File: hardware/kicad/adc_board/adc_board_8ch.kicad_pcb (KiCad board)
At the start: 2 copper layers, 88 x 66 mm, 10 parts, among them J1 ELECTRODES, J2 SPI_HOST, J3 PWR_CTRL, U1 ADS131M08

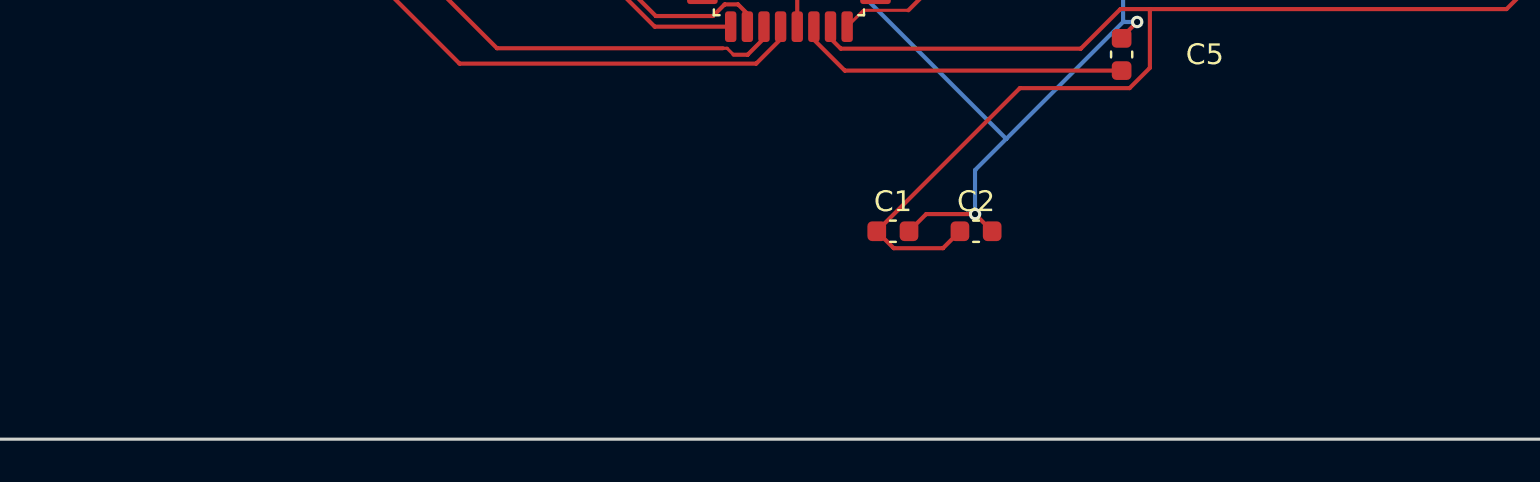
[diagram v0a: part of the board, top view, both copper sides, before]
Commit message: feat: add GND-tied fractal fill to ADC board
Co-authored-by: Copilot <223556219+Copilot@users.noreply.github.com>
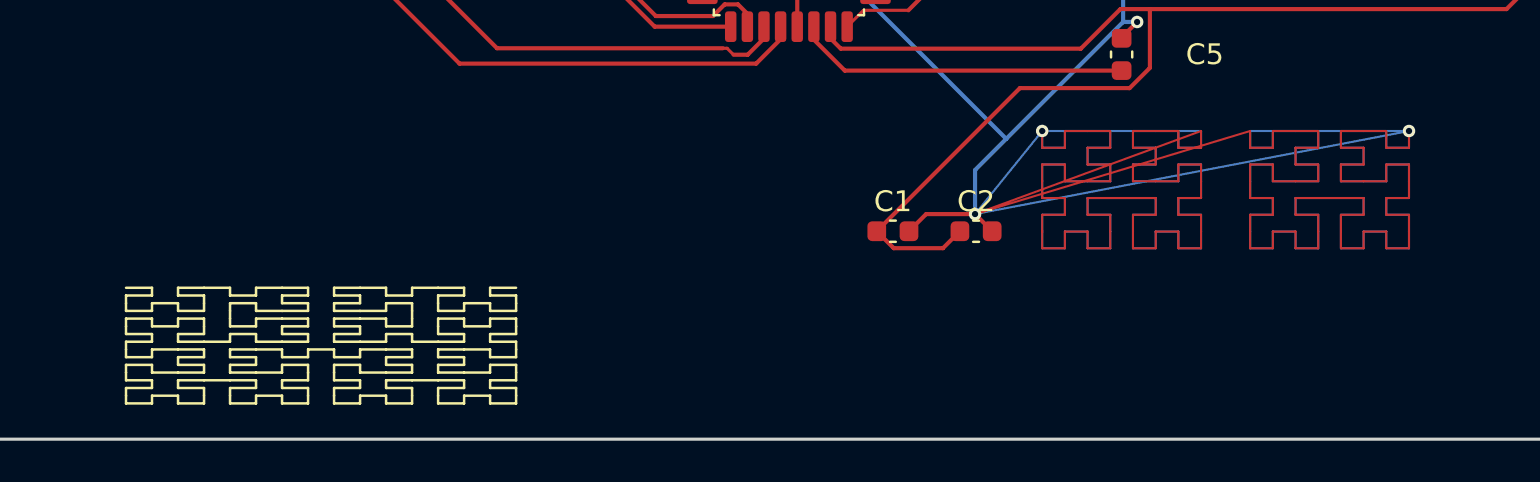
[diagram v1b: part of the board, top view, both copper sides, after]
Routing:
- net GND: track 92.8 -> 398.4 mm, vias 4 -> 6

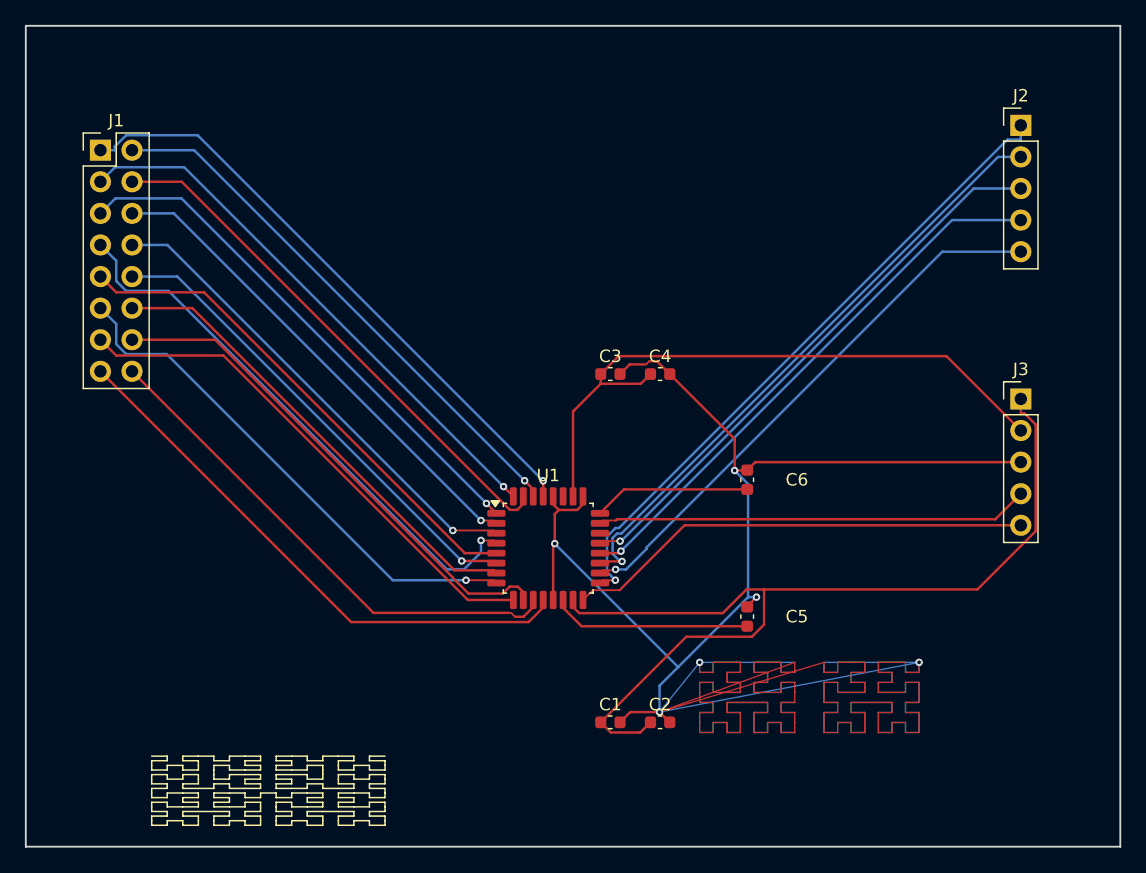
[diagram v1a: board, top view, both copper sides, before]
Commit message: fix(kicad): detect free space for ADC fractal fill
Co-authored-by: Copilot <223556219+Copilot@users.noreply.github.com>
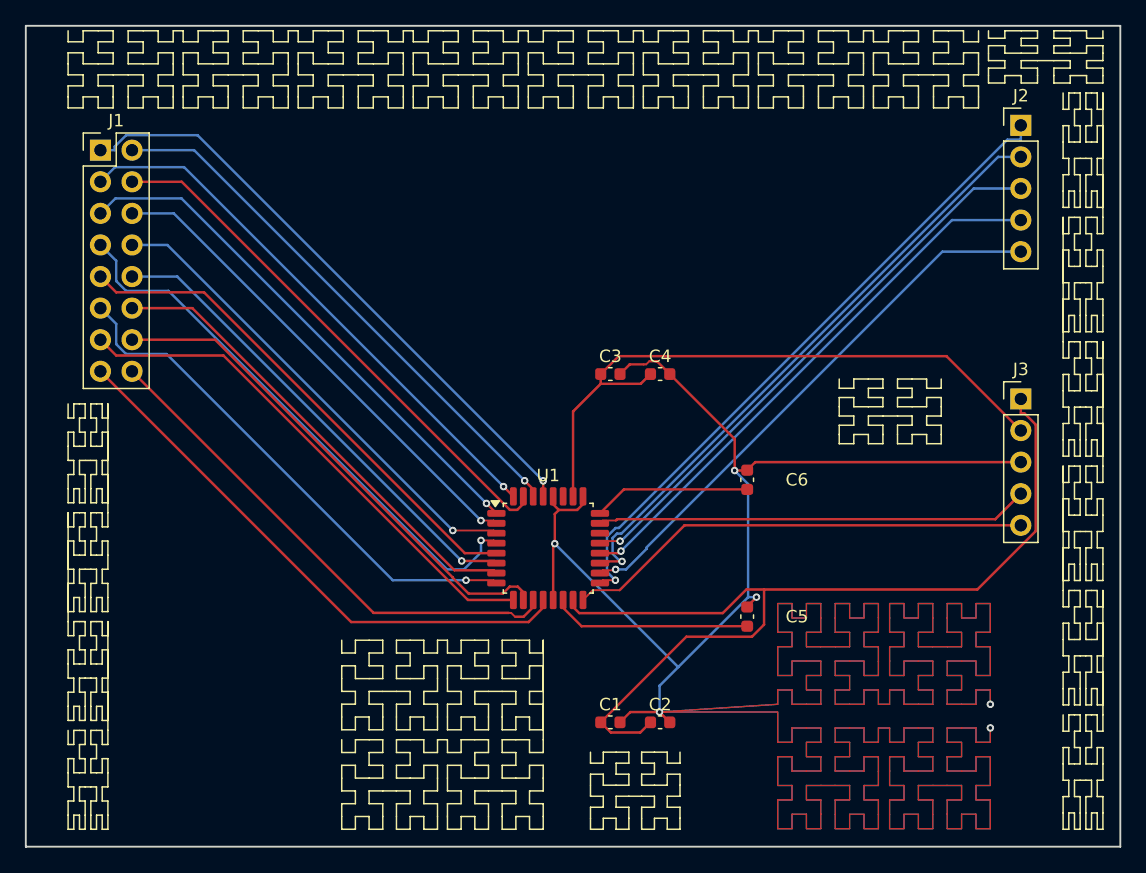
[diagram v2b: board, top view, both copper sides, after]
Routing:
- net GND: track 398.4 -> 720.2 mm

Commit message: fix(kicad): vary ADC fractal fill curves
Co-authored-by: Copilot <223556219+Copilot@users.noreply.github.com>
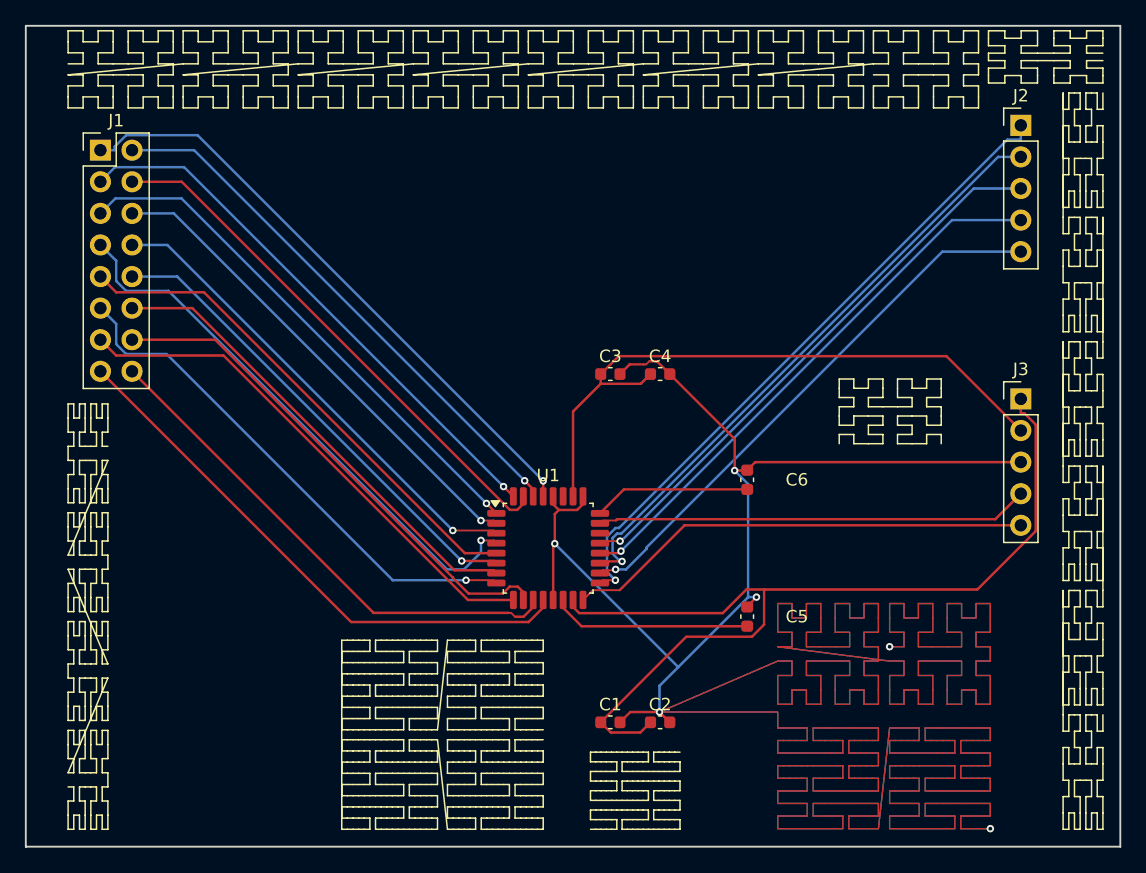
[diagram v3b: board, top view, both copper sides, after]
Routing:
- net GND: track 720.2 -> 810.8 mm

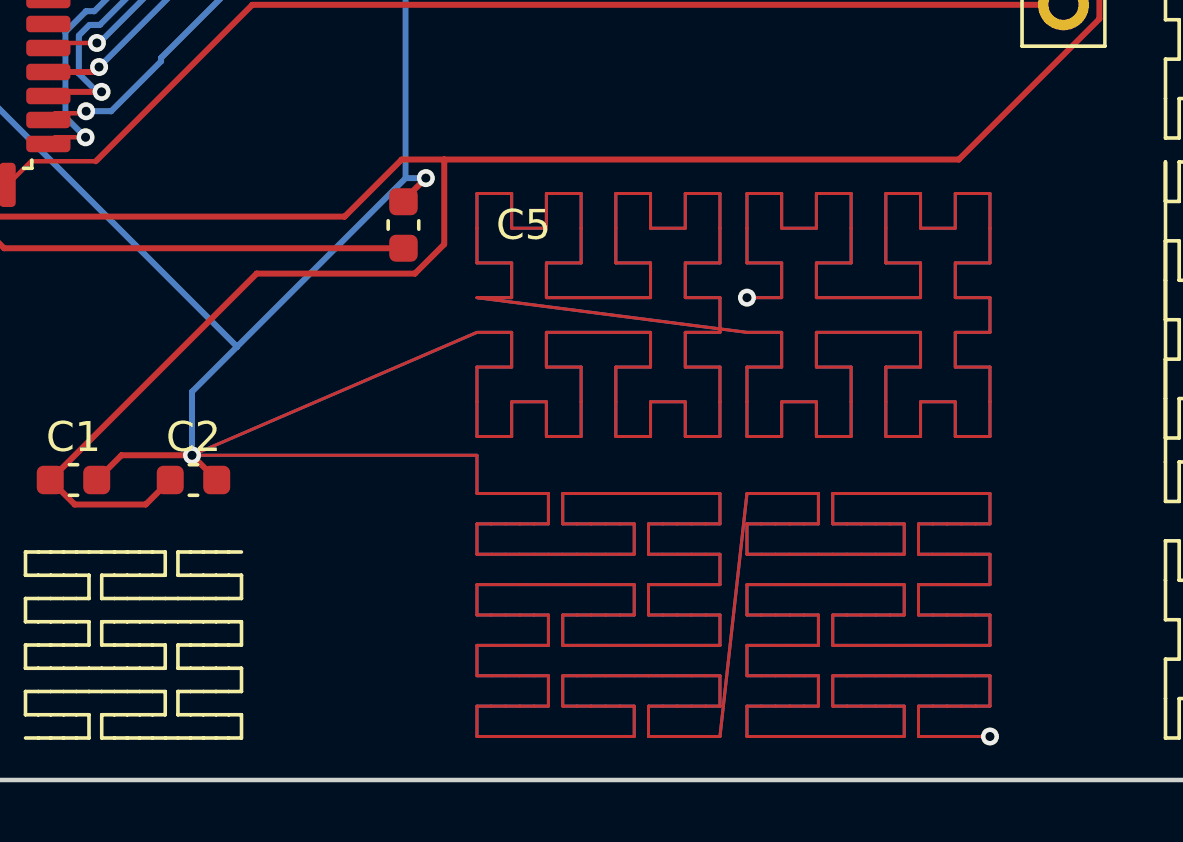
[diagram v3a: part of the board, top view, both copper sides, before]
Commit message: fix(kicad): pour ADC fractal fill as zones
Co-authored-by: Copilot <223556219+Copilot@users.noreply.github.com>
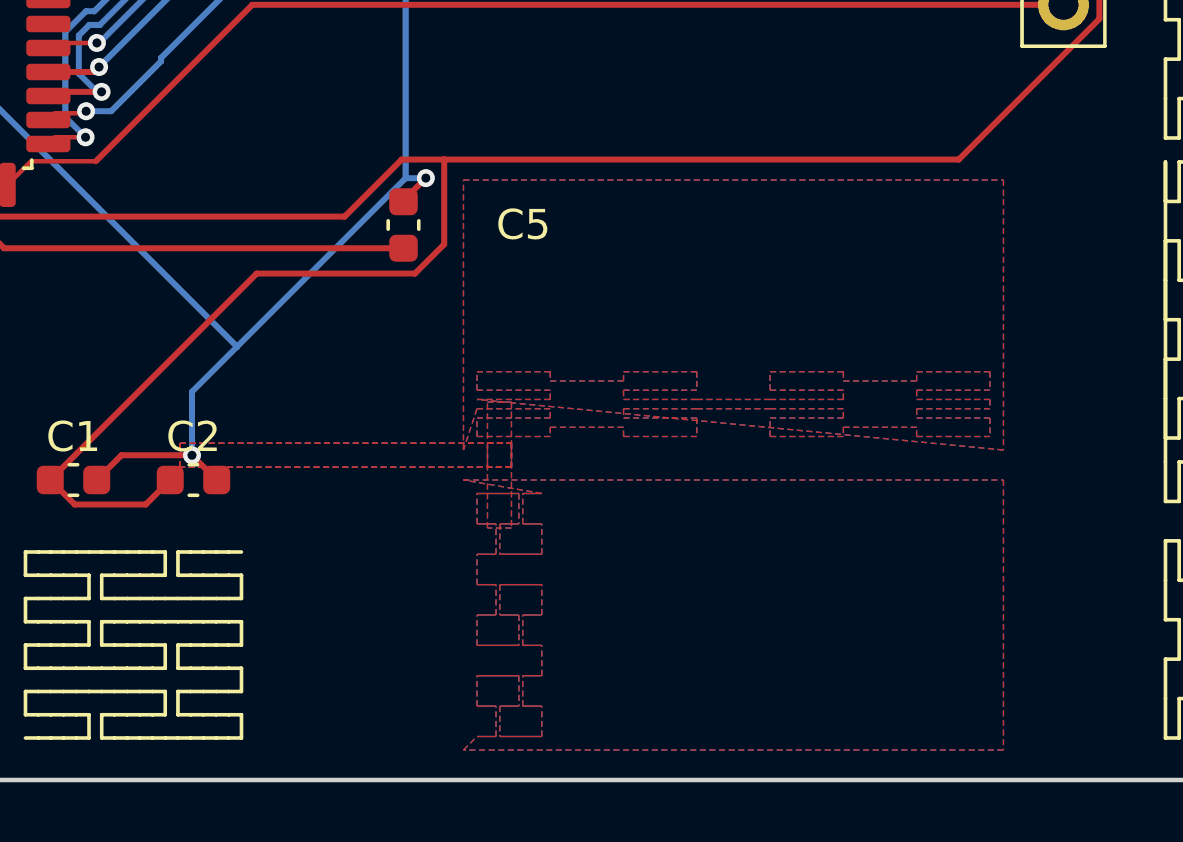
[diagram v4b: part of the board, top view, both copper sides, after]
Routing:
- net GND: track 810.8 -> 92.8 mm, vias 6 -> 4
- added copper zone on B.Cu, net GND
- added copper zone on F.Cu, net GND
